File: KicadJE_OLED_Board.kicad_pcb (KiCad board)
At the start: 2 copper layers, 40 x 128 mm, 39 parts, among them J1 LED 1-6, P1 Doepfer_Power_16pin

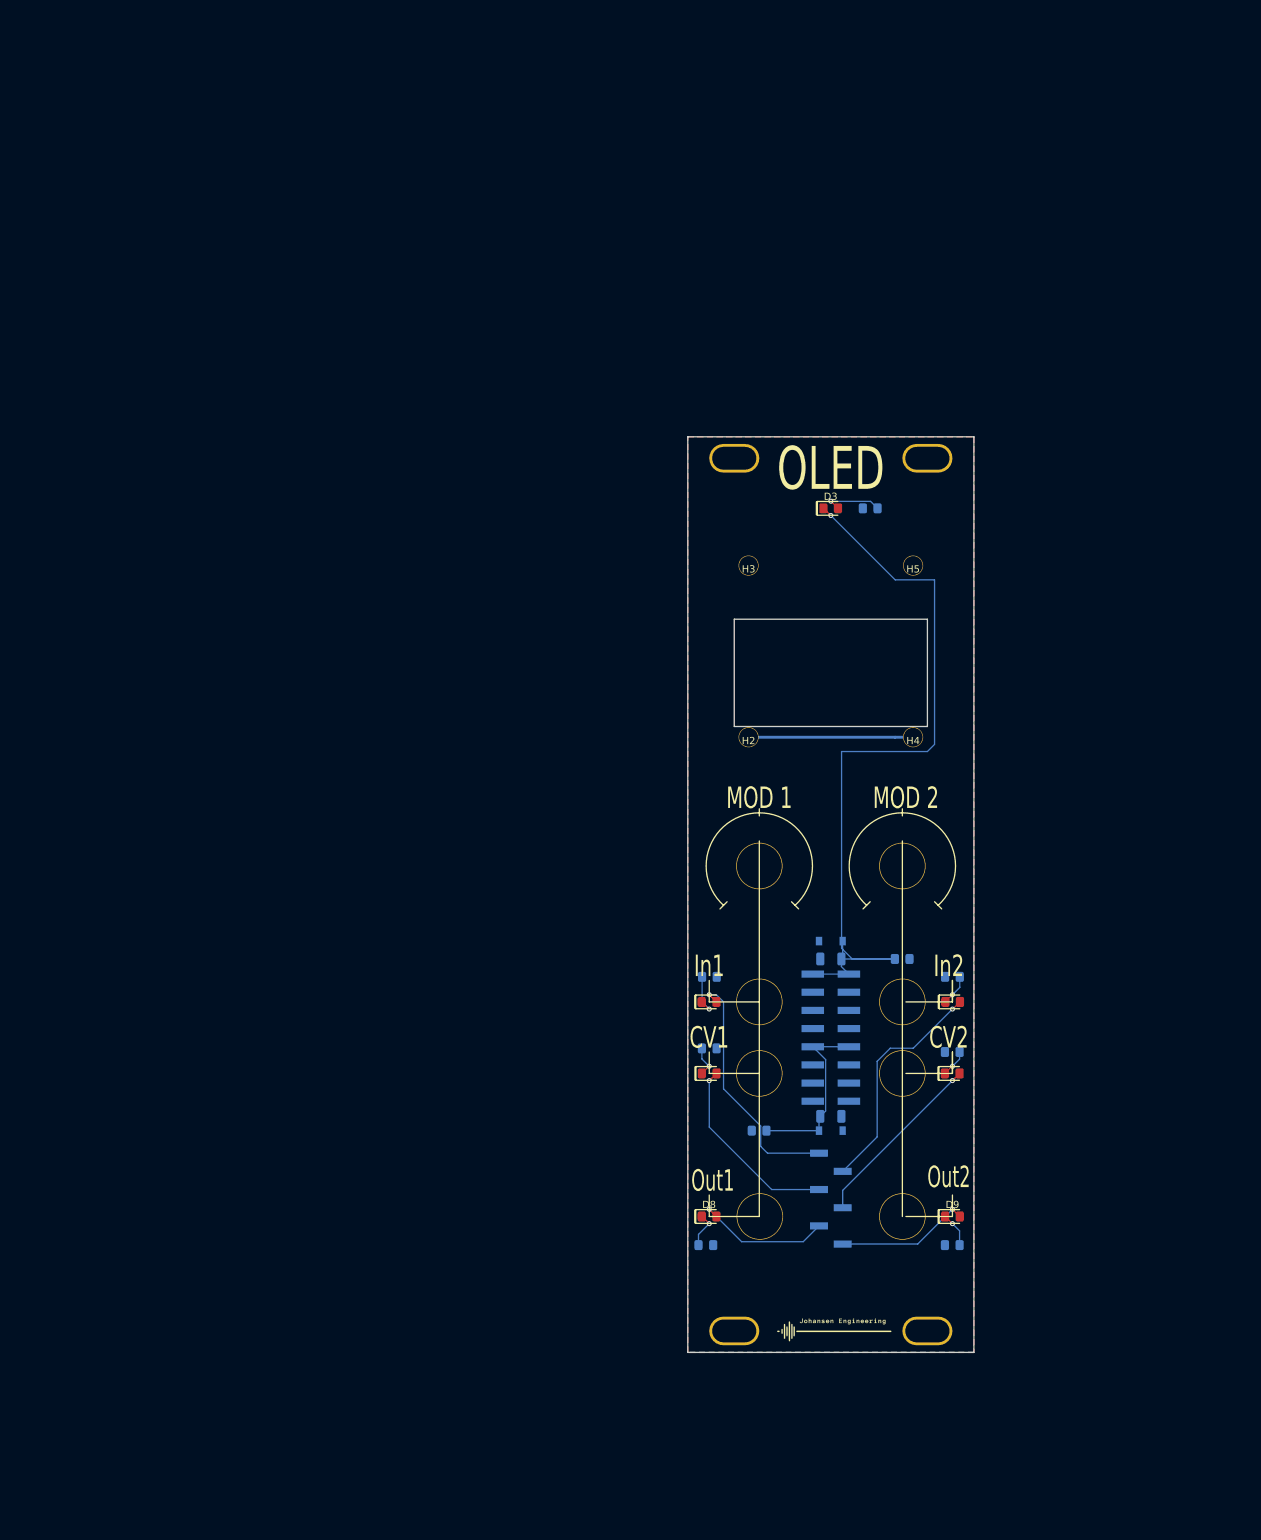
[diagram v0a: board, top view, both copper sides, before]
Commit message: PCB outline
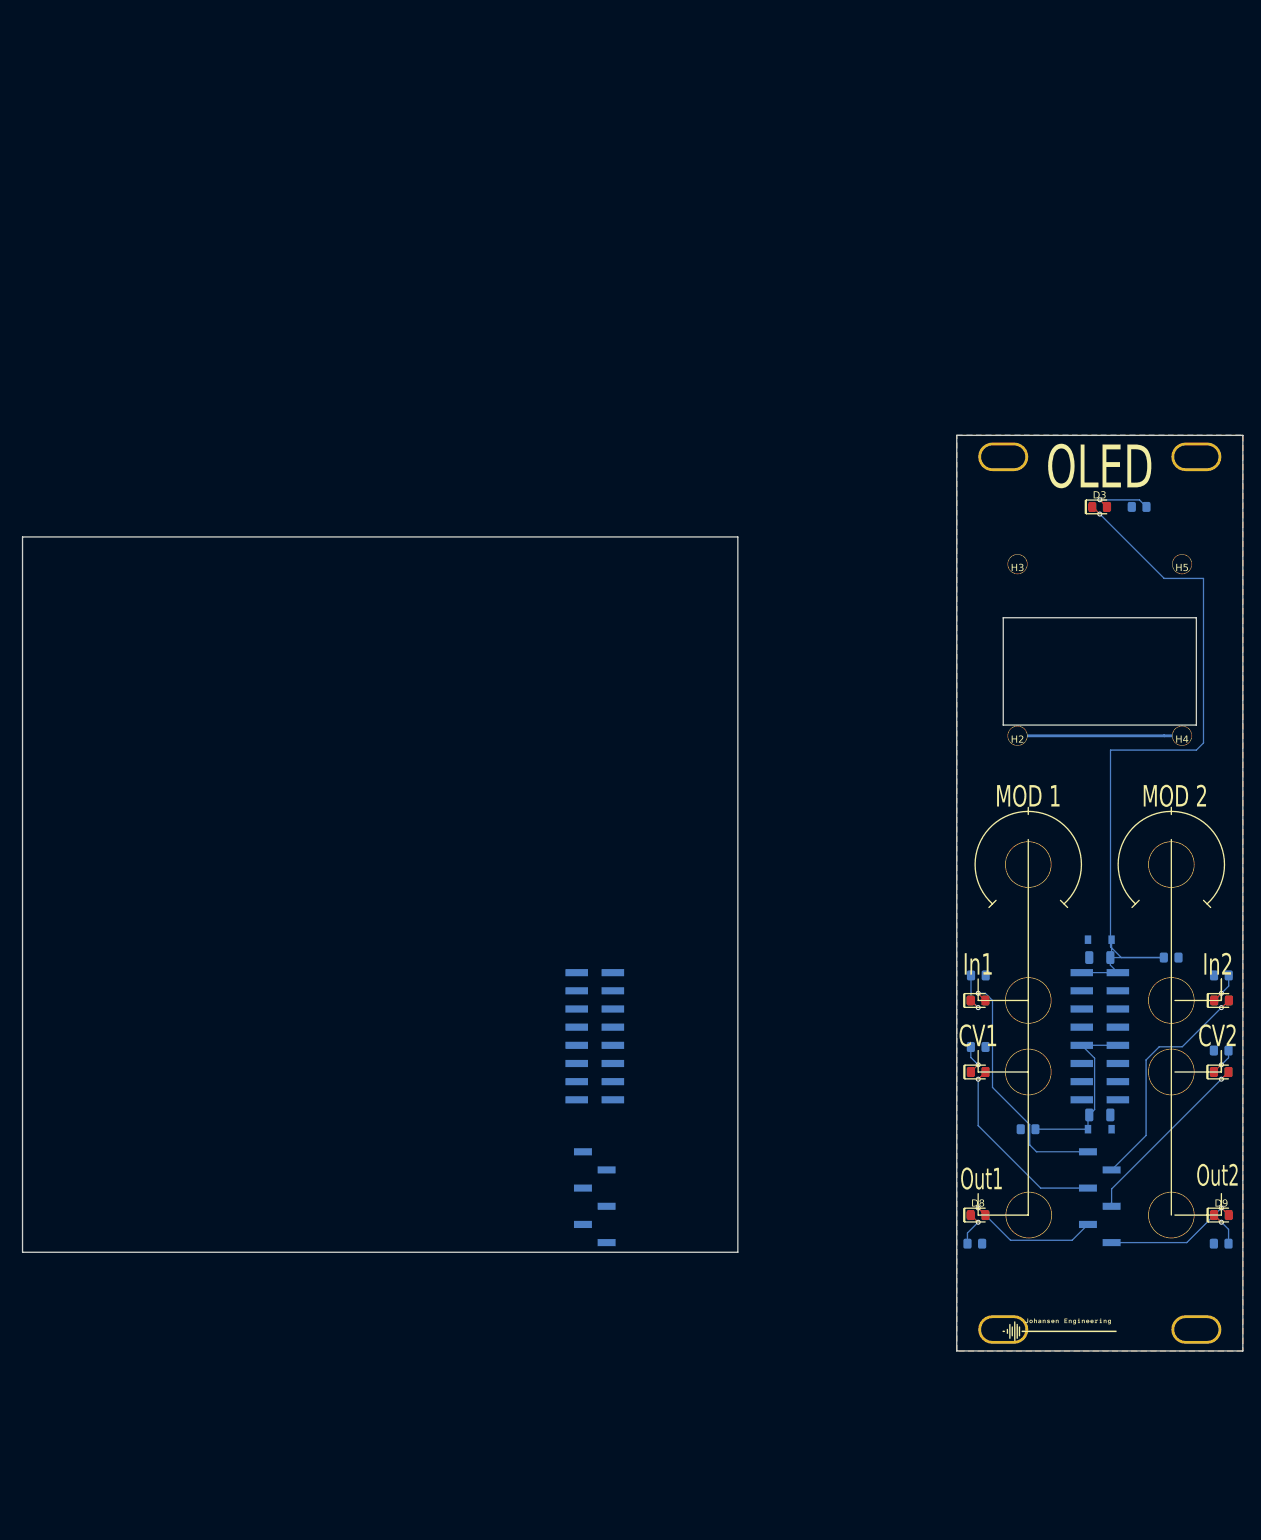
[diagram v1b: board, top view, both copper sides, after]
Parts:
- added J1: LED 1-6, Connector_PinHeader_2.54mm:PinHeader_1x06_P2.54mm_Vertical_SMD_Pin1Right, B.Cu at (180.0, 142.3)
- added P1: Doepfer_Power_16pin, Connector_PinHeader_2.54mm:PinHeader_2x08_P2.54mm_Vertical_SMD, B.Cu at (180.0, 119.8)
- moved D9 37.6 mm to (267.6, 144.8)
- moved H4 37.6 mm to (262.1, 77.8)
- moved H5 37.6 mm to (262.1, 53.8)
- moved H8 37.6 mm to (264.1, 160.8)
- moved H9 37.6 mm to (264.1, 38.8)
- moved R1 37.6 mm to (256.1, 45.8)
- moved R3 37.6 mm to (267.6, 111.3)
- moved TP103 37.6 mm to (260.6, 124.8)
- moved TP105 37.6 mm to (260.6, 144.8)
- moved TP106 37.6 mm to (240.7, 144.8)
- moved TP107 37.6 mm to (260.6, 95.8)
- moved TP107 37.6 mm to (260.6, 114.8)
- moved C1 37.6 mm to (250.6, 130.8)
- moved C2 37.6 mm to (250.6, 108.8)
- moved C3 37.6 mm to (240.6, 132.8)
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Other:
- board size 40 x 128 mm -> 170.6 x 128 mm

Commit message: Encoder 2
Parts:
- removed D3: LED, AJ:D_0805_AJ
- removed the J1 at (180.0, 142.3)
- removed the P1 at (180.0, 119.8)
- added C201: 1u, Capacitor_SMD:C_1206_3216Metric, B.Cu at (194.3, 41.5)
- added C202: 0R, AJ:C_0805_AJ, B.Cu at (197.6, 23.6)
- added C203: 0R, AJ:C_0805_AJ, B.Cu at (194.5, 38.3)
- added C204: 100n, Capacitor_SMD:C_1206_3216Metric, B.Cu at (189.3, 34.6)
- added C205: 100n, AJ:C_0805_AJ, B.Cu at (183.1, 27.5)
- added C206: 100n, AJ:C_0805_AJ, B.Cu at (199.5, 41.5)
- added C207: 1u, AJ:C_0805_AJ, B.Cu at (205.2, 45.0)
- added C208: 1u, AJ:C_0805_AJ, B.Cu at (183.0, 24.6)
- added C209: 1u, AJ:C_0805_AJ, B.Cu at (194.5, 35.4)
- added C210: 100n, AJ:C_0805_AJ, B.Cu at (199.3, 38.3)
- added C211: 100n, AJ:C_0805_AJ, B.Cu at (188.1, 27.6)
- added C212: 47n, AJ:C_0805_AJ, B.Cu at (192.8, 31.4)
- added C213: 100n, AJ:C_0805_AJ, B.Cu at (204.2, 41.5)
- added C214: 100n, AJ:C_0805_AJ, B.Cu at (210.0, 45.0)
- added C301: 100n, AJ:C_0805_AJ, B.Cu at (153.7, 170.1)
- added C302: 100n, AJ:C_0805_AJ, B.Cu at (158.5, 171.2)
- added C303: 100n, AJ:C_0805_AJ, B.Cu at (180.8, 187.5)
- added C304: 100n, AJ:C_0805_AJ, B.Cu at (175.1, 175.0)
- added C305: 100n, AJ:C_0805_AJ, B.Cu at (180.8, 184.6)
- added C306: 22p, AJ:C_0805_AJ, B.Cu at (163.2, 171.2)
- added C307: 22p, AJ:C_0805_AJ, B.Cu at (175.1, 180.9)
- added C308: 100n, AJ:C_0805_AJ, B.Cu at (175.1, 177.9)
- added D103: LED, AJ:D_SOD-123, F.Cu at (250.6, 45.8)
- added D104: 1N1007, AJ:D_SOD-123, B.Cu at (184.4, 16.0)
- added D105: 1N1007, AJ:D_SOD-123, B.Cu at (177.9, 6.13)
- added D106: 1N1007, AJ:D_SOD-123, B.Cu at (183.6, 9.48)
- added D107: 1N1007, AJ:D_SOD-123, B.Cu at (190.2, 16.0)
- added D108: 1N1007, AJ:D_SOD-123, B.Cu at (183.6, 6.13)
- added D109: 1N1007, AJ:D_SOD-123, B.Cu at (189.4, 12.7)
- added D110: 1N1007, AJ:D_SOD-123, B.Cu at (195.9, 16.0)
- added D111: 1N1007, AJ:D_SOD-123, B.Cu at (177.9, 9.48)
- added D201: 1N1007, AJ:D_SOD-123, B.Cu at (188.6, 44.8)
- added D202: 1N1007, AJ:D_SOD-123, B.Cu at (177.9, 37.1)
- added D203: 1N1007, AJ:D_SOD-123, B.Cu at (177.9, 33.7)
- added D204: 1N1007, AJ:D_SOD-123, B.Cu at (183.6, 37.1)
- added D205: 1N1007, AJ:D_SOD-123, B.Cu at (188.6, 41.5)
- added D206: 1N1007, AJ:D_SOD-123, B.Cu at (194.3, 44.8)
- added D207: 1N1007, AJ:D_SOD-123, B.Cu at (177.9, 30.4)
- added D208: 1N1007, AJ:D_SOD-123, B.Cu at (183.6, 33.7)
- added D209: LED, AJ:D_0805_AJ, B.Cu at (183.3, 30.5)
- added D301: LED, AJ:D_0805_AJ, B.Cu at (149.0, 170.1)
- added H101: ON, AJ:LED_Hole_3mm, B.Cu at (153.5, 24.0)
- added H2: OLED, AJ:M2.7_Plated, F.Cu at (168.6, 77.8)
- added H3: OLED, AJ:M2.7_Plated, F.Cu at (168.6, 53.8)
- added H4: OLED, AJ:M2.7_Plated, F.Cu at (191.6, 77.8)
- added H5: OLED, AJ:M2.7_Plated, F.Cu at (191.6, 53.8)
- added J201: OLED, Connector_PinSocket_2.54mm:PinSocket_1x04_P2.54mm_Vertical, F.Cu at (176.0, 78.0)
- added J202: IN1, AJ:PJ301SM, F.Cu at (170.0, 115.0)
- added J203: IN2, AJ:PJ301SM, F.Cu at (190.0, 115.0)
- added J204: CV1, AJ:PJ301SM, F.Cu at (170.0, 125.0)
- added J205: CV2, AJ:PJ301SM, F.Cu at (190.0, 125.0)
- added J206: FrontLED, Connector_PinSocket_2.54mm:PinSocket_1x06_P2.54mm_Vertical, F.Cu at (180.0, 135.8)
- added J207: ADC Input, Connector_PinSocket_2.54mm:PinSocket_1x06_P2.54mm_Vertical, F.Cu at (101.0, 27.5)
- added J208: -12V Front, Connector_PinSocket_2.54mm:PinSocket_1x02_P2.54mm_Vertical, F.Cu at (179.0, 113.5)
- added J209: Out2, Connector_PinSocket_2.54mm:PinSocket_1x02_P2.54mm_Vertical, B.Cu at (160.9, 12.1)
- added J210: Out1, Connector_PinSocket_2.54mm:PinSocket_1x02_P2.54mm_Vertical, B.Cu at (165.5, 12.1)
- added J211: OUT1, AJ:PJ301SM, F.Cu at (170.0, 145.0)
- added J212: OUT2, AJ:PJ301SM, F.Cu at (190.0, 145.0)
- added J301: UART, Connector_PinHeader_2.54mm:PinHeader_1x06_P2.54mm_Vertical, B.Cu at (148.7, 186.7)
- added J302: AVR-ISP-6, Connector_PinHeader_2.54mm:PinHeader_2x03_P2.54mm_Vertical, B.Cu at (167.8, 180.0)
- added JP201: 1, Jumper:SolderJumper-3_P1.3mm_Bridged12_Pad1.0x1.5mm_NumberLabels, B.Cu at (189.3, 38.0)
- added JP202: 2, Jumper:SolderJumper-3_P1.3mm_Bridged12_Pad1.0x1.5mm_NumberLabels, B.Cu at (177.8, 26.9)
- added JP203: 3, Jumper:SolderJumper-3_P1.3mm_Bridged12_Pad1.0x1.5mm_NumberLabels, B.Cu at (200.0, 44.7)
- added JP204: 4, Jumper:SolderJumper-3_P1.3mm_Bridged12_Pad1.0x1.5mm_NumberLabels, B.Cu at (177.8, 23.4)
- added P201: Doepfer_Power_16pin, Connector_IDC:IDC-Header_2x08_P2.54mm_Vertical, B.Cu at (171.5, 59.5)
- added R102: 10k, AJ:R_0805_AJ, B.Cu at (183.9, 12.9)
- added R103: 10k, AJ:R_0805_AJ, B.Cu at (188.9, 9.53)
- added R104: 10k, AJ:R_0805_AJ, B.Cu at (188.9, 6.58)
- added R105: 10k, AJ:R_0805_AJ, B.Cu at (194.6, 12.9)
- added R113: 10k, AJ:R_0805_AJ, B.Cu at (194.6, 9.93)
- added R114: 10k, AJ:R_0805_AJ, B.Cu at (188.9, 3.63)
- added R115: 10k, AJ:R_0805_AJ, B.Cu at (193.6, 6.98)
- added R116: 10k, AJ:R_0805_AJ, B.Cu at (199.4, 12.9)
- added R201: 10R, AJ:R_0805_AJ, B.Cu at (187.9, 24.7)
- added R202: 10R, AJ:R_0805_AJ, B.Cu at (199.3, 35.4)
- added R203: 10R, AJ:R_0805_AJ, B.Cu at (188.1, 30.6)
- added R204: 10R, AJ:R_0805_AJ, B.Cu at (197.6, 26.5)
- added R205: 10k, AJ:R_0805_AJ, B.Cu at (213.7, 42.1)
- added R206: 10k, AJ:R_0805_AJ, B.Cu at (202.3, 32.4)
- added R207: 10k, AJ:R_0805_AJ, B.Cu at (208.8, 38.5)
- added R208: 1k, AJ:R_0805_AJ, B.Cu at (204.0, 35.6)
- added R209: OPEN, AJ:R_0805_AJ, B.Cu at (197.6, 29.5)
- added R210: OPEN, AJ:R_0805_AJ, B.Cu at (197.6, 32.4)
- added R211: 10k, AJ:R_0805_AJ, B.Cu at (209.0, 42.1)
- added R212: 10k, AJ:R_0805_AJ, B.Cu at (192.8, 25.5)
- added R213: 20k, AJ:R_0805_AJ, B.Cu at (211.8, 29.7)
- added R214: 20k, AJ:R_0805_AJ, B.Cu at (202.3, 23.6)
- added R215: 20k, AJ:R_0805_AJ, B.Cu at (192.8, 28.5)
- added R216: 20k, AJ:R_0805_AJ, B.Cu at (207.1, 23.8)
- added R217: 1k, AJ:R_0805_AJ, B.Cu at (207.1, 26.7)
- added R218: 1k, AJ:R_0805_AJ, B.Cu at (214.7, 45.0)
- added R219: 10k, AJ:R_0805_AJ, B.Cu at (211.8, 32.6)
- added R220: 20k, AJ:R_0805_AJ, B.Cu at (218.3, 39.1)
- added R221: 20k, AJ:R_0805_AJ, B.Cu at (213.5, 36.2)
- added R222: 1k, AJ:R_0805_AJ, B.Cu at (207.1, 29.7)
- added R223: 1k, AJ:R_0805_AJ, B.Cu at (192.6, 22.6)
- added R224: 10k, AJ:R_0805_AJ, B.Cu at (202.3, 26.5)
- added R225: 10R, AJ:R_0805_AJ, B.Cu at (207.1, 32.6)
- added R226: 10R, AJ:R_0805_AJ, B.Cu at (213.5, 39.1)
- added R227: 10R, AJ:R_0805_AJ, B.Cu at (208.8, 35.6)
- added R228: 22k, AJ:R_0805_AJ, B.Cu at (202.3, 29.5)
- added R229: 10k, AJ:R_0805_AJ, B.Cu at (204.0, 38.5)
- added R301: 0R, AJ:R_0805_AJ, B.Cu at (168.0, 171.2)
- added R302: 0R, Jumper:SolderJumper-2_P1.3mm_Bridged_RoundedPad1.0x1.5mm, B.Cu at (172.5, 170.9)
- added R303: 10k, AJ:R_0805_AJ, B.Cu at (180.8, 181.6)
- added R304: 1k, AJ:R_0805_AJ, B.Cu at (153.7, 173.1)
- added R305: OPEN, AJ:R_0805_AJ, B.Cu at (179.8, 178.7)
- added SW201: Rotary_Encoder_Switch, Rotary_Encoder:RotaryEncoder_Alps_EC11E-Switch_Vertical_H20mm, F.Cu at (172.5, 88.5)
- added TP201: Flow1, TestPoint:TestPoint_THTPad_2.0x2.0mm_Drill1.0mm, B.Cu at (217.9, 35.6)
- added TP202: Flow2, TestPoint:TestPoint_THTPad_2.0x2.0mm_Drill1.0mm, B.Cu at (211.5, 26.2)
- added U201: TL072, AJ:AJ_SO-8_5.3x6.2mm_P1.27mm, B.Cu at (180.4, 42.6)
- added U301: ATmega32A-AU, Package_QFP:TQFP-44_10x10mm_P0.8mm, B.Cu at (158.3, 181.8)
- added Y301: 16MHz, Crystal:Crystal_HC49-U_Vertical, B.Cu at (169.5, 185.7)
- moved G*** 5.00 mm to (250.0, 161.0)
- renumbered C1 to C101, C2 to C102, C3 to C103, C4 to C104, D1 to D101, D2 to D102, H7 to H102, H6 to H103, H9 to H104, H8 to H105, R1 to R101
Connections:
- R101 pad 1: GND -> Net-(D103-Pad2)
- R101 pad 2: Net-(D3-Pad2) -> GND
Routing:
- net Net-(D3-Pad2): track 8.35 -> 0.00 mm, vias 1 -> 0
- net GND: track 23.0 -> 31.4 mm, vias 0 -> 1

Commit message: Component place
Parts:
- removed the J207 at (101.0, 27.5)
- added C201: 0R, AJ:C_0805_AJ, F.Cu at (109.4, 2.23)
- added C202: 0R, AJ:C_0805_AJ, F.Cu at (127.9, -13.0)
- added C207: 0R, AJ:C_0805_AJ, F.Cu at (114.1, 2.23)
- added C208: 0R, AJ:C_0805_AJ, F.Cu at (127.9, -10.1)
- added C210: 100n, AJ:C_0805_AJ, F.Cu at (132.7, -13.0)
- added C212: 100n, AJ:C_0805_AJ, F.Cu at (118.9, 2.23)
- added C219: 47n, AJ:C_0805_AJ, F.Cu at (127.9, -7.12)
- added J202: ADC Input, Connector_PinSocket_2.54mm:PinSocket_1x03_P2.54mm_Vertical, F.Cu at (101.0, 27.5)
- added R209: OPEN, AJ:R_0805_AJ, F.Cu at (132.7, -10.1)
- added R210: OPEN, AJ:R_0805_AJ, F.Cu at (137.4, -13.0)
- added R226: 10k, AJ:R_0805_AJ, F.Cu at (127.9, -4.17)
- added R230: 10k, AJ:R_0805_AJ, F.Cu at (123.6, 2.23)
- added R234: 10k, AJ:R_0805_AJ, F.Cu at (132.7, -7.12)
- added SW202: Rotary_Encoder_Switch, Rotary_Encoder:RotaryEncoder_Alps_EC11E-Switch_Vertical_H20mm, F.Cu at (192.5, 88.5)
- renumbered C202 to C203, C203 to C204, C201 to C205, C204 to C206, C205 to C209, C206 to C211, C207 to C213, C208 to C214, C209 to C215, C210 to C216, C211 to C217, C212 to C218, C213 to C220, C214 to C221, J209 to J203, J210 to J204, J211 to J205, J212 to J206, J202 to J207, J203 to J208, J204 to J209, J205 to J210, J206 to J211, J208 to J212, R113 to R106, R114 to R107, R115 to R108, R116 to R109, R211 to R205, R212 to R208, R209 to R211, R210 to R212, R205 to R213, R208 to R214, R213 to R215, R214 to R216, R215 to R217, R216 to R218, R217 to R219, R218 to R220, R220 to R221, R221 to R222, R222 to R223, R223 to R224, R219 to R225, R225 to R227, R226 to R228, R224 to R229, R227 to R231, R228 to R232, R229 to R233
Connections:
- R205 pad 2: 27_A3 -> Net-(C201-Pad1)
- R208 pad 2: 28_A4 -> Net-(C202-Pad1)
- R223 pad 1: Out1_32 -> Net-(C207-Pad1)
- R224 pad 1: Out2_32 -> Net-(C208-Pad1)
